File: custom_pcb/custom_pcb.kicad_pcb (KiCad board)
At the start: 2 copper layers, 285 x 152 mm, 312 parts, among them J1 USB_mini_micro_B, K0 KEYSW, K1 KEYSW, K10 KEYSW, K11 KEYSW, K12 KEYSW, K13 KEYSW, K14 KEYSW, K15 KEYSW, K16 KEYSW, K17 KEYSW, K18 KEYSW, K19 KEYSW, K2 KEYSW, K20 KEYSW, K21 KEYSW, K22 KEYSW, K23 KEYSW, K24 KEYSW, K25 KEYSW, K26 KEYSW, K27 KEYSW, K28 KEYSW, K29 KEYSW, K3 KEYSW, K30 KEYSW, K31 KEYSW, K32 KEYSW, K33 KEYSW, K34 KEYSW, K35 KEYSW, K36 KEYSW, K37 KEYSW, K38 KEYSW, K39 KEYSW, K4 KEYSW, K40 KEYSW, K41 KEYSW, K42 KEYSW, K43 KEYSW, K44 KEYSW, K45 KEYSW, K46 KEYSW, K47 KEYSW, K48 KEYSW, K49 KEYSW, K5 KEYSW, K50 KEYSW, K51 KEYSW, K52 KEYSW, K53 KEYSW, K54 KEYSW, K55 KEYSW, K56 KEYSW, K57 KEYSW, K58 KEYSW, K59 KEYSW, K60 KEYSW, K63 KEYSW, K64 KEYSW, K65 KEYSW, K66 KEYSW, K67 KEYSW, K68 KEYSW, K69 KEYSW, K7 KEYSW, K70 KEYSW, K71 KEYSW, K72 KEYSW, K73 KEYSW, K74 KEYSW, K75 KEYSW, K76 KEYSW, K77 KEYSW, K78 KEYSW, K79 KEYSW, K8 KEYSW, K80 KEYSW, K81 KEYSW, K82 KEYSW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

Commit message: logic for rest in parallel, but ultimately go with series since the setup is safer if the attempt fails, also consdering trying to put everything on the front for real smd
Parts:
- added K6: KEYSW, cherry_rgb:CHERRY_PLATE_91.6H, F.Cu at (148.2, 54.0)
- added R16: R, Resistors_SMD:R_0603_HandSoldering, B.Cu at (150.2, 68.8)
- added R17: R, Resistors_SMD:R_0603_HandSoldering, B.Cu at (150.2, 74.0)
- added SW1: CONN_02X02, Buttons_Switches_SMD:SW_DIP_x2_W5.08mm_Slide_Copal_CHS-A, B.Cu at (146.8, 72.5)
- moved RE0 20.1 mm to (147.0, 66.5)
- moved RE2 18.8 mm to (145.5, 66.5)
- moved D47 8.85 mm to (203.5, 128.5), turned to 270 degrees
- moved D26 8.68 mm to (170.2, 90.6), turned to 270 degrees
- moved D43 8.50 mm to (127.2, 128.5), turned to 90 degrees
- moved D36 8.31 mm to (175.0, 109.8), turned to 270 degrees
- moved D46 7.83 mm to (184.5, 128.5)
- moved D53 3.12 mm to (112.4, 149.5), turned to 180 degrees
- moved D52 3.01 mm to (93.2, 149.5), turned to 180 degrees
- moved RE1 2.55 mm to (145.5, 66.5)
- moved R5 2.37 mm to (145.2, 62.8), turned to 0 degrees
- moved D55 0.25 mm to (217.0, 151.5)
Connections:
- LC0 pad 20: OFF? -> (no net)
- LC2 pad 10: OFF? -> (no net)
- RE0 pad 2: GND -> rec
- RE1 pad 2: GND -> rec
- RE2 pad 2: GND -> rec
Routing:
- net Net-(LC0-Pad23): track 35.3 -> 59.7 mm, vias 1 -> 3
- net Net-(LC2-Pad23): track 31.3 -> 41.1 mm, vias 1 -> 3
- net rec: track 0.00 -> 7.24 mm, vias 0 -> 1
- net Net-(R16-Pad2): track 0.00 -> 5.96 mm
- net anode0: track 176.6 -> 174.7 mm
- net Net-(LC1-Pad23): track 16.1 -> 17.6 mm
- net +3V3: track 178.4 -> 179.4 mm
- net r1: vias 12 -> 11
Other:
- net class Default: clearance 0.2 -> 0.16
- net class Power Default added: clearance 0.2, trace_width 0.5, via_dia 1, via_drill 0.5
- net class anodes added: clearance 0.2, trace_width 0.4, via_dia 0.8, via_drill 0.4
- net class cols added: clearance 0.2, trace_width 0.5, via_dia 1, via_drill 0.5
- net class column diodes added: clearance 0.2, trace_width 0.5, via_dia 1, via_drill 0.5
- net class power removed
- net class rows added: clearance 0.2, trace_width 0.5, via_dia 1, via_drill 0.5
- rule trace_clearance: 0.2 -> 0.16

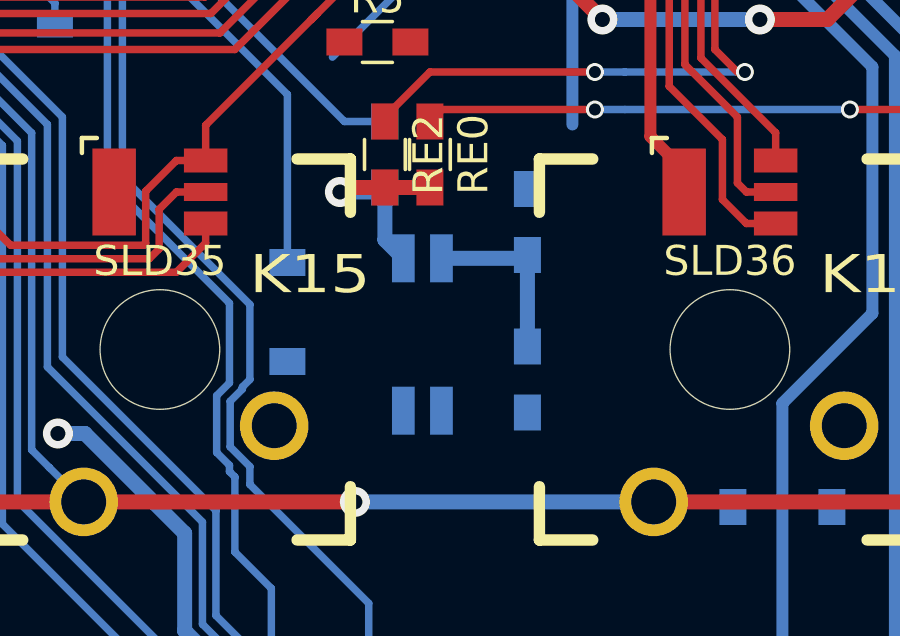
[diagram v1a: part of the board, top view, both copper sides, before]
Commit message: cpcb footprint for the 2 DIP switch
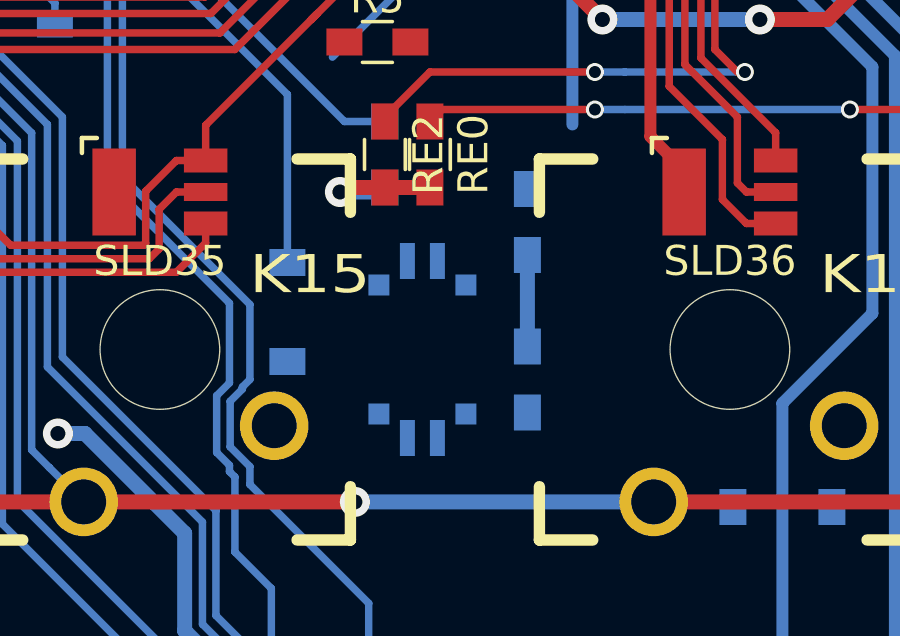
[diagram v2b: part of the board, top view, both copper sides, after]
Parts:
- SW1: footprint Buttons_Switches_SMD:SW_DIP_x2_W5.08mm_Slide_Copal_CHS-A -> cherry_rgb:CVS-02TB
- moved SW1 0.50 mm to (146.8, 73.0), turned to 180 degrees
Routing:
- net Net-(R16-Pad2): track 5.96 -> 0.16 mm
- net GND: track 21.3 -> 24.4 mm
- net rec: track 7.24 -> 4.62 mm

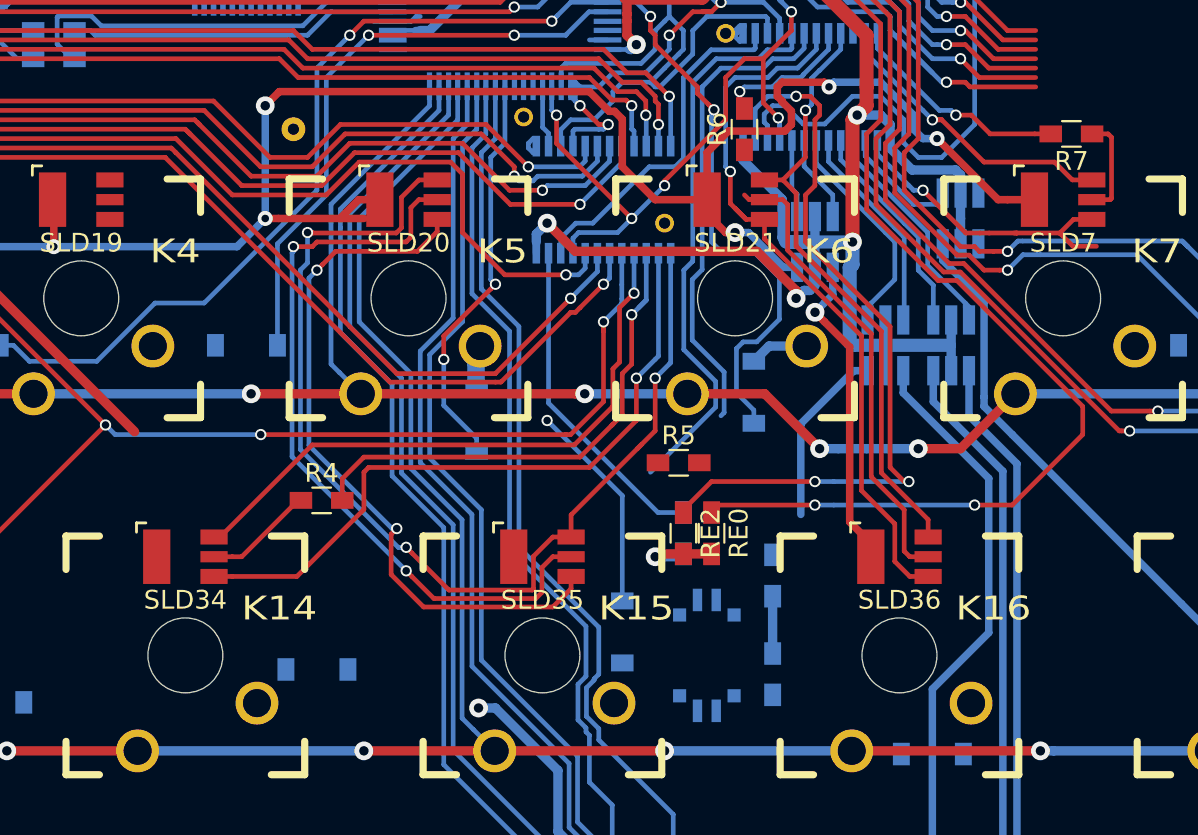
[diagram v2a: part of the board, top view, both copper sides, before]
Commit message: routing tweaks for gnd plane
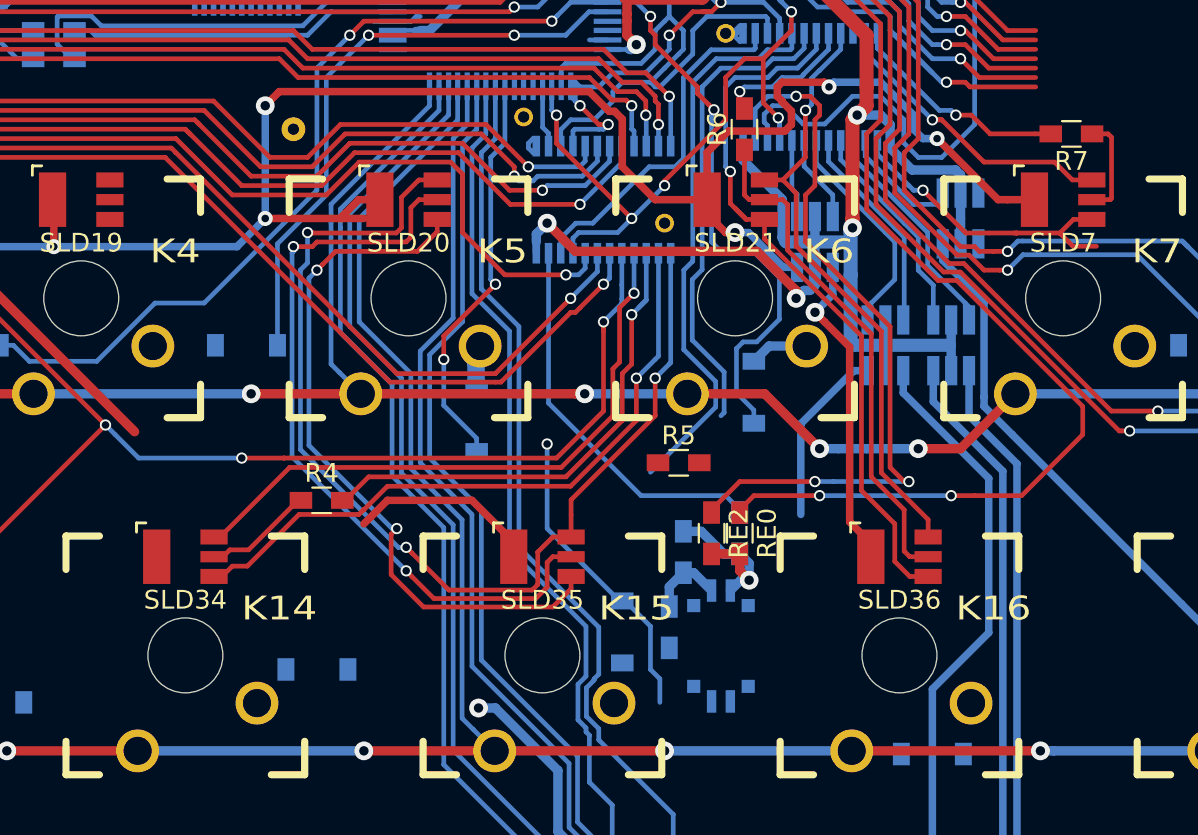
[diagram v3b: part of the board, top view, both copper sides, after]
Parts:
- moved R17 6.04 mm to (144.8, 71.5)
- moved R16 4.91 mm to (145.5, 67.5)
- moved RE1 3.00 mm to (148.5, 66.5)
- moved RE0 1.50 mm to (148.5, 66.5)
- moved RE2 1.50 mm to (147.0, 66.5)
- moved SW1 0.90 mm to (147.5, 72.5)
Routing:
- net anode1: track 17.0 -> 27.2 mm
- net c5: track 33.1 -> 38.1 mm
- net rec: track 4.62 -> 9.44 mm
- net Net-(R16-Pad2): track 0.16 -> 4.00 mm
- net Net-(LC1-Pad23): track 17.6 -> 20.7 mm
- net GND: track 24.4 -> 21.3 mm
- net red6: track 24.9 -> 27.3 mm
- net Net-(LC2-Pad23): track 41.1 -> 39.6 mm
- net Net-(LC0-Pad23): track 59.7 -> 58.3 mm
- net green3: track 74.3 -> 75.6 mm
- net green4: track 36.5 -> 35.3 mm
- net +3V3: track 179.4 -> 178.5 mm
- net Net-(LC1-Pad15): track 27.2 -> 26.7 mm

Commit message: tweaks
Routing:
- net c4: track 31.8 -> 50.6 mm
- net green5: track 67.7 -> 64.6 mm
- net Net-(LC1-Pad19): track 45.6 -> 47.9 mm
- net green2: track 69.5 -> 67.7 mm
- net anode0: track 174.7 -> 173.4 mm
- net blue3: track 53.1 -> 54.2 mm
- net Net-(LC1-Pad15): track 26.7 -> 26.1 mm

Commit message: tweaks
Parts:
- moved R5 1.80 mm to (143.8, 63.8), turned to 90 degrees
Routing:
- net red5: track 40.3 -> 46.1 mm
- net Net-(LC2-Pad6): track 25.6 -> 28.3 mm, vias 0 -> 1
- net anode1: track 27.2 -> 26.0 mm
- net c11: track 34.8 -> 33.7 mm
- net blue5: track 57.9 -> 57.2 mm
- net c0: track 109.8 -> 109.2 mm

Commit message: more tweaks
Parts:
- moved R12 0.25 mm to (256.1, 33.5)
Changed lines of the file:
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@@
     (thickness 1.6)
     (drawings 6)
-    (tracks 1961)
+    (tracks 1958)
     (zones 0)
     (modules 316)
@@
   )
   (module Resistors_SMD:R_0603_HandSoldering (layer F.Cu)
-    (at 256.1 33.25)
+    (at 256.1 33.5)
     (descr "Resistor SMD 0603, hand soldering")
     (tags "resistor 0603")
@@
   (segment (start 122.364999 67.385001) (end 125 64.75) (width 0.25) (layer F.Cu) (net 122))
   (segment (start 125 64.75) (end 125.15 64.75) (width 0.25) (layer F.Cu) (net 122))
+  (segment (start 124.75 51.25) (end 126.3 51.25) (width 0.25) (layer F.Cu) (net 123))
+  (segment (start 126.5 51.05) (end 130.65 51.05) (width 0.25) (layer F.Cu) (net 123))
+  (segment (start 130.65 51.05) (end 131 50.7) (width 0.25) (layer F.Cu) (net 123))
+  (segment (start 131 50.7) (end 131 49.175) (width 0.25) (layer F.Cu) (net 123))
+  (segment (start 131 49.175) (end 131.425 48.75) (width 0.25) (layer F.Cu) (net 123))
+  (segment (start 126.3 51.25) (end 126.5 51.05) (width 0.25) (layer F.Cu) (net 123))
+  (segment (start 131.425 48.75) (end 132.4 48.75) (width 0.25) (layer F.Cu) (net 123))
   (via (at 131.25 69) (size 0.6) (drill 0.4) (layers F.Cu B.Cu) (net 123))
   (segment (start 132.3 70.05) (end 131.25 69) (width 0.25) (layer F.Cu) (net 123))
@@
   (segment (start 124.75 51.25) (end 124.75 55.5) (width 0.25) (layer B.Cu) (net 123))
   (segment (start 124.75 55.5) (end 125.25 56) (width 0.25) (layer B.Cu) (net 123))
-  (segment (start 130.5 51) (end 126 51) (width 0.25) (layer F.Cu) (net 123))
-  (segment (start 131 49.175) (end 131 50.5) (width 0.25) (layer F.Cu) (net 123))
-  (segment (start 130.5 51) (end 131 50.5) (width 0.25) (layer F.Cu) (net 123))
   (segment (start 139.525 67.75) (end 138.55 67.75) (width 0.25) (layer F.Cu) (net 123))
   (segment (start 138.55 67.75) (end 138.25 68.05) (width 0.25) (layer F.Cu) (net 123))
-  (segment (start 125.75 51.25) (end 124.75 51.25) (width 0.25) (layer F.Cu) (net 123))
-  (segment (start 126 51) (end 125.75 51.25) (width 0.25) (layer F.Cu) (net 123))
   (via (at 124.75 51.25) (size 0.6) (drill 0.4) (layers F.Cu B.Cu) (net 123))
-  (segment (start 132.4 48.75) (end 131.425 48.75) (width 0.25) (layer F.Cu) (net 123))
-  (segment (start 131.425 48.75) (end 131 49.175) (width 0.25) (layer F.Cu) (net 123))
   (segment (start 148.75 48.5) (end 148.75 46.1) (width 0.25) (layer F.Cu) (net 124))
   (segment (start 149.81667 48.75) (end 150.79167 48.75) (width 0.25) (layer F.Cu) (net 124))
@@
   (via (at 142.875 53.728357) (size 0.6) (drill 0.4) (layers F.Cu B.Cu) (net 141))
   (segment (start 142.875 51.6) (end 142.875 53.728357) (width 0.25) (layer B.Cu) (net 141))
-  (segment (start 138.425 70.55) (end 136 70.55) (width 0.25) (layer F.Cu) (net 142))
-  (segment (start 132.75 70.75) (end 135.8 70.75) (width 0.25) (layer F.Cu) (net 142))
-  (segment (start 135.8 70.75) (end 136 70.55) (width 0.25) (layer F.Cu) (net 142))
-  (via (at 132.75 70.75) (size 0.6) (drill 0.4) (layers F.Cu B.Cu) (net 142))
+  (segment (start 132.4 49.8) (end 132.4 50.45) (width 0.25) (layer F.Cu) (net 142))
+  (segment (start 132.4 50.45) (end 131.3 51.55) (width 0.25) (layer F.Cu) (net 142))
+  (segment (start 131.3 51.55) (end 126.95 51.55) (width 0.25) (layer F.Cu) (net 142))
+  (segment (start 126.95 51.55) (end 126 52.5) (width 0.25) (layer F.Cu) (net 142))
   (segment (start 139.525 68.8) (end 139.525 69.45) (width 0.25) (layer F.Cu) (net 142))
   (segment (start 139.525 69.45) (end 138.425 70.55) (width 0.25) (layer F.Cu) (net 142))
+  (segment (start 138.425 70.55) (end 132.95 70.55) (width 0.25) (layer F.Cu) (net 142))
+  (segment (start 132.95 70.55) (end 132.75 70.75) (width 0.25) (layer F.Cu) (net 142))
+  (via (at 132.75 70.75) (size 0.6) (drill 0.4) (layers F.Cu B.Cu) (net 142))
   (segment (start 132.75 65.75) (end 132.75 70.75) (width 0.25) (layer B.Cu) (net 142))
   (segment (start 129.5 62.5) (end 132.75 65.75) (width 0.25) (layer B.Cu) (net 142))
@@
   (segment (start 147.215359 59.784641) (end 145.75 61.25) (width 0.25) (layer B.Cu) (net 142))
   (segment (start 126 52.5) (end 126.25 52.75) (width 0.25) (layer B.Cu) (net 142))
-  (segment (start 131.35 51.5) (end 127 51.5) (width 0.25) (layer F.Cu) (net 142))
-  (segment (start 126 52.5) (end 126.299999 52.200001) (width 0.25) (layer F.Cu) (net 142))
-  (segment (start 126.299999 52.200001) (end 127 51.5) (width 0.25) (layer F.Cu) (net 142))
   (via (at 126 52.5) (size 0.6) (drill 0.4) (layers F.Cu B.Cu) (net 142))
-  (segment (start 132.4 50.45) (end 131.35 51.5) (width 0.25) (layer F.Cu) (net 142))
-  (segment (start 132.4 49.8) (end 132.4 50.45) (width 0.25) (layer F.Cu) (net 142))
+  (segment (start 132.4 47.7) (end 131.425 47.7) (width 0.25) (layer F.Cu) (net 143))
+  (segment (start 131.425 47.7) (end 130.5 48.625) (width 0.25) (layer F.Cu) (net 143))
+  (segment (start 130.5 48.625) (end 130.5 50.35) (width 0.25) (layer F.Cu) (net 143))
+  (segment (start 130.5 50.35) (end 130.3 50.55) (width 0.25) (layer F.Cu) (net 143))
+  (segment (start 130.3 50.55) (end 125.578367 50.55) (width 0.25) (layer F.Cu) (net 143))
+  (segment (start 125.578367 50.55) (end 125.493357 50.46499) (width 0.25) (layer F.Cu) (net 143))
+  (segment (start 125.25 55.25) (end 125.25 52) (width 0.25) (layer B.Cu) (net 143))
+  (segment (start 125.493357 50.889254) (end 125.493357 50.46499) (width 0.25) (layer B.Cu) (net 143))
+  (segment (start 125.493357 51.756643) (end 125.493357 50.889254) (width 0.25) (layer B.Cu) (net 143))
+  (segment (start 125.25 52) (end 125.493357 51.756643) (width 0.25) (layer B.Cu) (net 143))
+  (segment (start 125.75 55.75) (end 125.25 55.25) (width 0.25) (layer B.Cu) (net 143))
+  (segment (start 132 68.25) (end 132 65.75) (width 0.25) (layer B.Cu) (net 143))
+  (segment (start 132 65.75) (end 125.75 59.5) (width 0.25) (layer B.Cu) (net 143))
+  (via (at 125.493357 50.46499) (size 0.6) (drill 0.4) (layers F.Cu B.Cu) (net 143))
+  (segment (start 125.75 59.5) (end 125.75 55.75) (width 0.25) (layer B.Cu) (net 143))
   (segment (start 137.75 69.25) (end 137.75 67.5) (width 0.25) (layer F.Cu) (net 143))
   (segment (start 137.45 69.55) (end 137.75 69.25) (width 0.25) (layer F.Cu) (net 143))
@@
   (segment (start 132 68.25) (end 133.3 69.55) (width 0.25) (layer F.Cu) (net 143))
   (via (at 132 68.25) (size 0.6) (drill 0.4) (layers F.Cu B.Cu) (net 143))
-  (segment (start 132 65.75) (end 132 68.25) (width 0.25) (layer B.Cu) (net 143))
-  (segment (start 127.5 61.25) (end 132 65.75) (width 0.25) (layer B.Cu) (net 143))
-  (segment (start 125.75 55.75) (end 125.75 59.5) (width 0.25) (layer B.Cu) (net 143))
-  (segment (start 125.75 59.5) (end 127.5 61.25) (width 0.25) (layer B.Cu) (net 143))
   (segment (start 144.825 51.6) (end 144.825 55.5) (width 0.25) (layer B.Cu) (net 143))
   (segment (start 144.825 55.5) (end 144.825 55.675) (width 0.25) (layer B.Cu) (net 143))
@@
   (segment (start 139.525 64.725) (end 143.25 61) (width 0.25) (layer F.Cu) (net 143))
   (segment (start 143.25 61) (end 143.25 58.25) (width 0.25) (layer F.Cu) (net 143))
-  (segment (start 125.5 50.5) (end 125.5 51.75) (width 0.25) (layer B.Cu) (net 143))
-  (segment (start 125.5 51.75) (end 125.25 52) (width 0.25) (layer B.Cu) (net 143))
-  (segment (start 125.25 52) (end 125.25 55.25) (width 0.25) (layer B.Cu) (net 143))
-  (segment (start 125.25 55.25) (end 125.75 55.75) (width 0.25) (layer B.Cu) (net 143))
   (segment (start 139.525 65.525) (end 139.525 64.725) (width 0.25) (layer F.Cu) (net 143))
   (segment (start 138.55 66.7) (end 137.75 67.5) (width 0.25) (layer F.Cu) (net 143))
-  (segment (start 132.4 47.7) (end 131.425 47.7) (width 0.25) (layer F.Cu) (net 143))
-  (segment (start 130.224999 50.525001) (end 125.775001 50.525001) (width 0.25) (layer F.Cu) (net 143))
-  (segment (start 131.425 47.7) (end 130.5 48.625) (width 0.25) (layer F.Cu) (net 143))
-  (segment (start 125.775001 50.525001) (end 125.75 50.5) (width 0.25) (layer F.Cu) (net 143))
-  (segment (start 130.5 48.625) (end 130.5 50.25) (width 0.25) (layer F.Cu) (net 143))
-  (segment (start 130.5 50.25) (end 130.224999 50.525001) (width 0.25) (layer F.Cu) (net 143))
-  (segment (start 125.75 50.5) (end 125.5 50.5) (width 0.25) (layer F.Cu) (net 143))
-  (via (at 125.5 50.5) (size 0.6) (drill 0.4) (layers F.Cu B.Cu) (net 143))
   (segment (start 139.525 65.525) (end 139.525 66.7) (width 0.25) (layer F.Cu) (net 143))
   (segment (start 139.525 66.7) (end 138.55 66.7) (width 0.25) (layer F.Cu) (net 143))

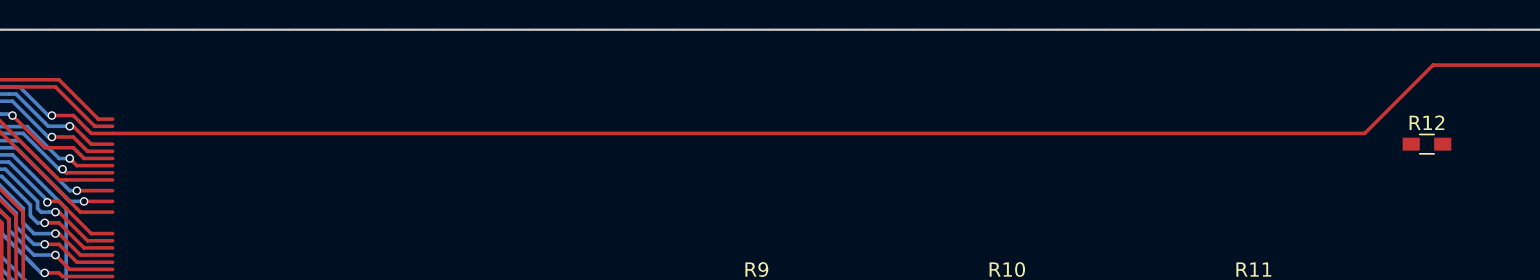
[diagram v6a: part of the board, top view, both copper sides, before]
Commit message: tweak was correct this time >_<
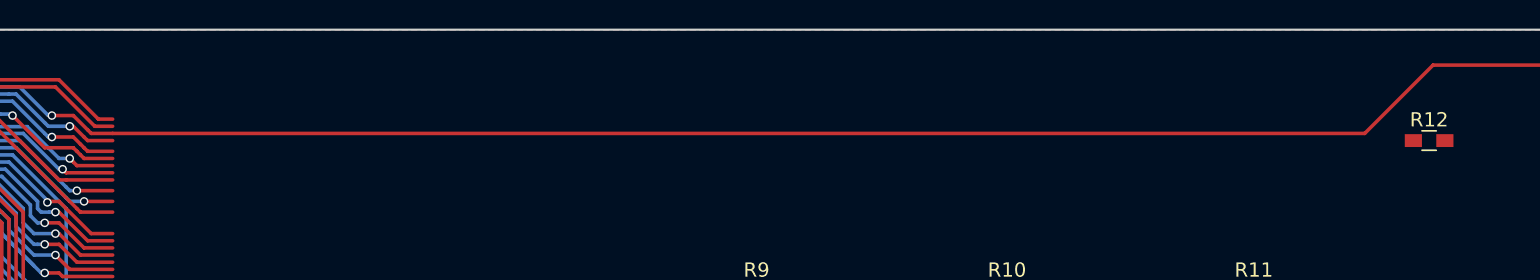
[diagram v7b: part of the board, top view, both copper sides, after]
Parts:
- moved R12 0.29 mm to (256.2, 33.2)
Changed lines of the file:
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@@
     (thickness 1.6)
     (drawings 6)
-    (tracks 1958)
+    (tracks 1957)
     (zones 0)
     (modules 316)
@@
   )
   (module Resistors_SMD:R_0603_HandSoldering (layer F.Cu)
-    (at 256.1 33.5)
+    (at 256.25 33.25)
     (descr "Resistor SMD 0603, hand soldering")
     (tags "resistor 0603")
@@
   (segment (start 153.300001 32.275001) (end 158.275001 32.275001) (width 0.25) (layer B.Cu) (net 198))
   (segment (start 158.275001 32.275001) (end 159.75 33.75) (width 0.25) (layer B.Cu) (net 198))
-  (segment (start 162.75 33.5) (end 164.25 33.5) (width 0.25) (layer F.Cu) (net 199))
-  (segment (start 162.5 33.25) (end 162.75 33.5) (width 0.25) (layer F.Cu) (net 199))
+  (segment (start 162.5 33.25) (end 164.25 33.25) (width 0.25) (layer F.Cu) (net 199))
   (segment (start 162.5 33.25) (end 162.25 33) (width 0.25) (layer F.Cu) (net 199))
   (segment (start 162.25 33) (end 161.5 32.25) (width 0.25) (layer F.Cu) (net 199))

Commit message: columns wired
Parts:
- moved V5 11.6 mm to (132.0, 36.0)
- moved D43 0.56 mm to (127.8, 128.8), turned to 270 degrees
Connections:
- U1 pad 56: c5 -> r2
- U1 pad 57: r2 -> r5
- U1 pad 58: r5 -> c5
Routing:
- net c8: track 54.3 -> 165.0 mm
- net c3: track 44.5 -> 154.8 mm
- net c12: track 35.3 -> 144.0 mm
- net c0: track 109.2 -> 214.0 mm
- net c2: track 62.7 -> 166.3 mm
- net c1: track 77.0 -> 179.6 mm
- net c11: track 33.7 -> 135.3 mm
- net c9: track 97.4 -> 188.4 mm
- net c10: track 116.2 -> 203.2 mm
- net c7: track 51.5 -> 133.7 mm
- net c4: track 50.6 -> 122.6 mm
- net c13: track 32.4 -> 103.2 mm
- net c14: track 30.6 -> 98.9 mm
- net c5: track 38.1 -> 83.1 mm, vias 3 -> 2
- net c6: track 32.8 -> 76.9 mm
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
